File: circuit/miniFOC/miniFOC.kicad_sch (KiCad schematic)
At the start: 82 parts, among them J1 Conn_01x05, J2 Conn_01x03, J3 Conn_01x04, J4 Conn_01x02, J5 Conn_01x01, J6 Conn_01x01, J7 Conn_01x01, Q1 RU30J30M, Q2 RU30J30M, Q3 RU30J30M, U1 XC6206P332MR, U2 CH32V203C8T6, U3 LM321, U4 COS722MR, U5 BDR2L00, U6 BDR2L00, U7 BDR2L00, U8 JW5017S

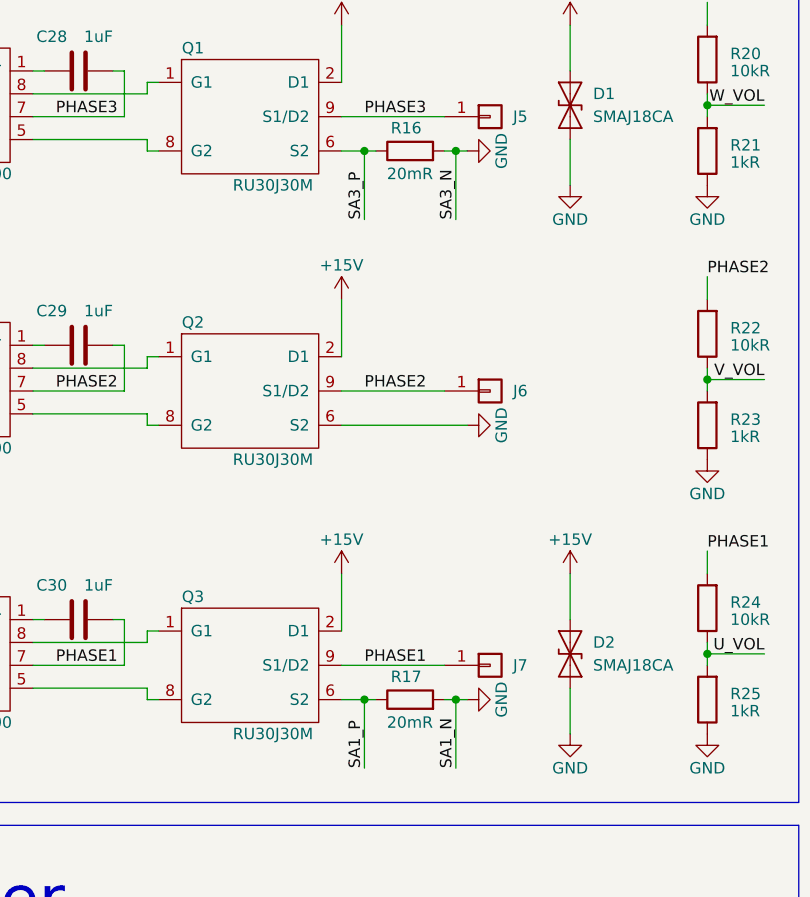
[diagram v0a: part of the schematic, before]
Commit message: Modify the sampling resistor package in the schematic diagram and PCB, and change its resistance value to 5 milliohms to adapt to the current sampling range of 20A.
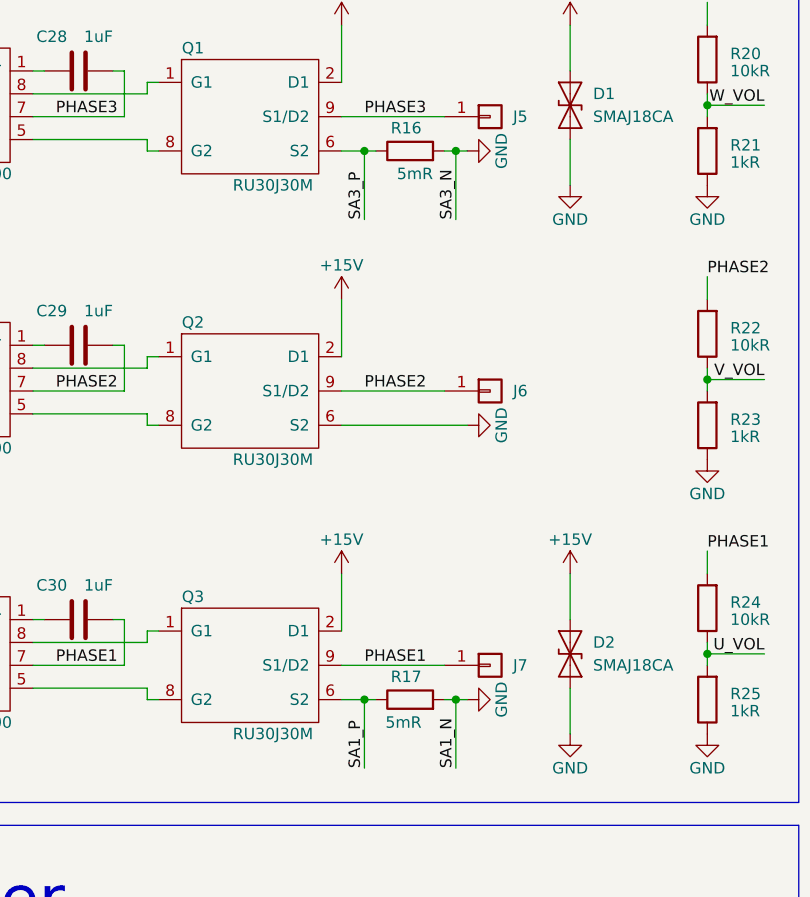
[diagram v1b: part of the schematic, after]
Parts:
- R16, R17: value 20mR -> 5mR; footprint library:R_0805_2012Metric -> library:R_1206_3216Metric
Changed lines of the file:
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@@
   (title_block
     (title "miniFOC")
-    (date "2023-06-20")
+    (date "2023-06-24")
     (rev "2.0.1")
   )
@@
       (effects (font (size 1.27 1.27)) (justify left))
     )
-    (property "Value" "20mR" (at 242.57 48.26 90)
+    (property "Value" "5mR" (at 242.57 48.26 90)
       (effects (font (size 1.27 1.27)) (justify left))
     )
-    (property "Footprint" "library:R_0805_2012Metric" (at 240.03 47.498 90)
+    (property "Footprint" "library:R_1206_3216Metric" (at 240.03 47.498 90)
       (effects (font (size 1.27 1.27)) hide)
     )
@@
       (effects (font (size 1.27 1.27)) (justify left))
     )
-    (property "Value" "20mR" (at 242.57 109.22 90)
+    (property "Value" "5mR" (at 241.3 109.22 90)
       (effects (font (size 1.27 1.27)) (justify left))
     )
-    (property "Footprint" "library:R_0805_2012Metric" (at 240.03 108.458 90)
+    (property "Footprint" "library:R_1206_3216Metric" (at 240.03 108.458 90)
       (effects (font (size 1.27 1.27)) hide)
     )

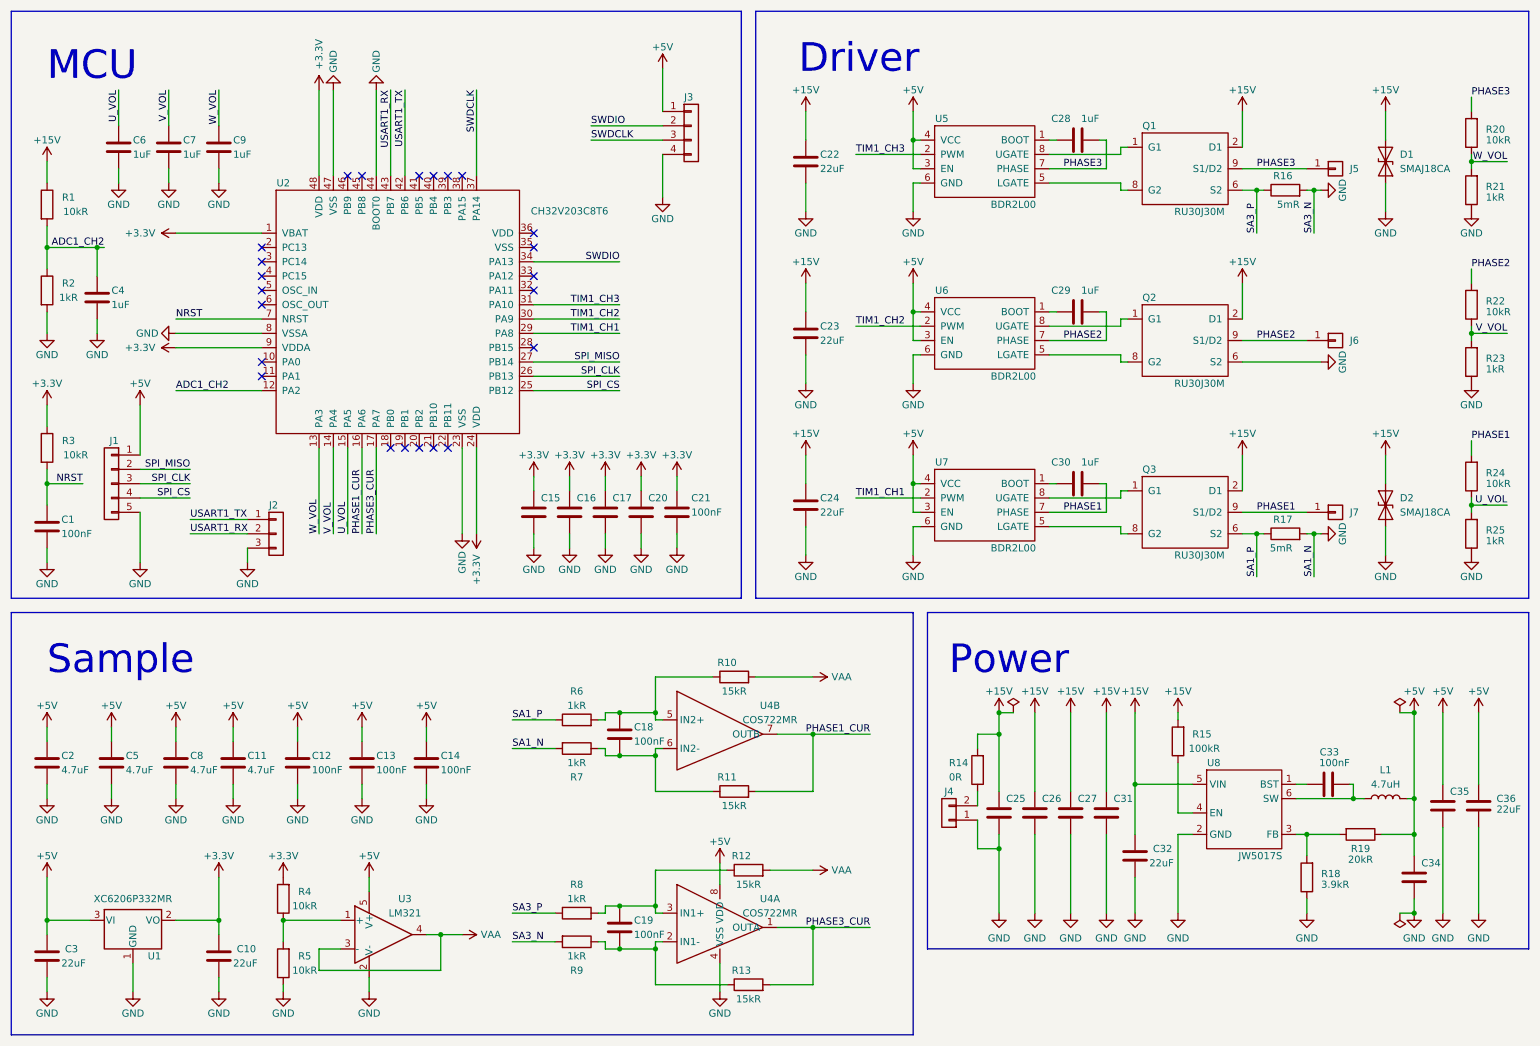
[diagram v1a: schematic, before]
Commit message: Updated PCB and schematic libraries to add buffer capacitors for current sampling.
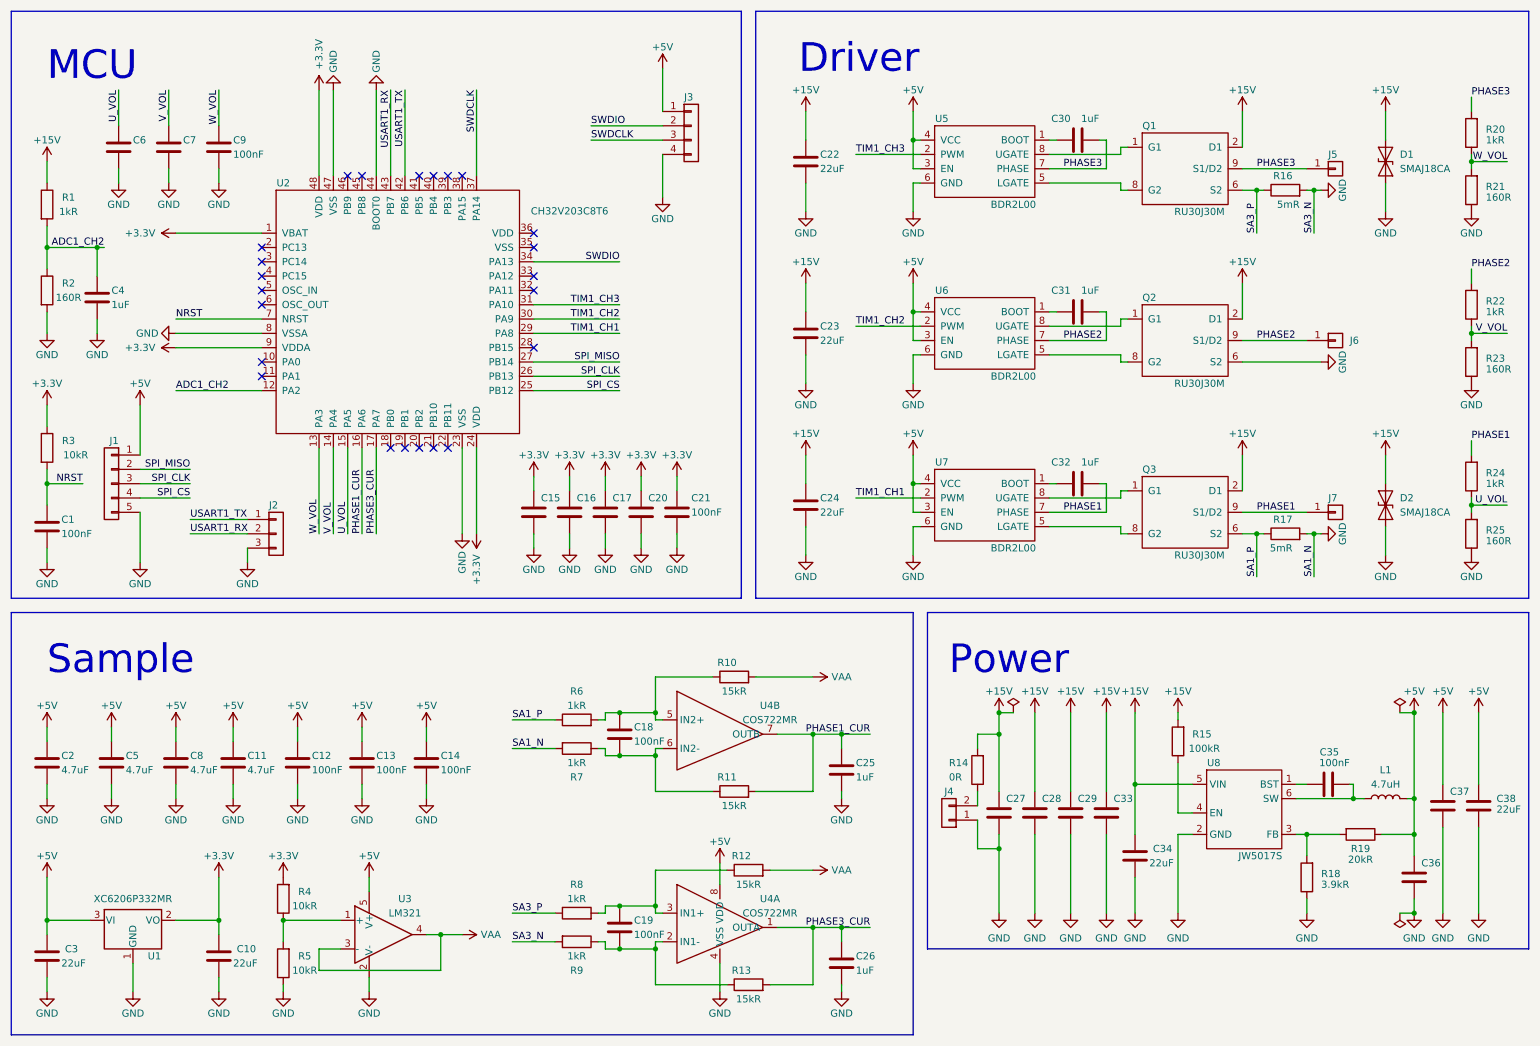
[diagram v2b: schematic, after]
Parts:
- added C25, C26: 1uF, library:C_0402_1005Metric, symbol library:C
- C6, C7, C9: value 1uF -> 100nF
- R1, R20, R22, R24: value 10kR -> 1kR
- R2, R21, R23, R25: value 1kR -> 160R
- renumbered C25 to C27, C26 to C28, C27 to C29, C28 to C30, C29 to C31, C30 to C32, C31 to C33, C32 to C34, C33 to C35, C34 to C36, C35 to C37, C36 to C38
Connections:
- net EP: now also C25.2, C26.2
- net PHASE1_CUR: now also C25.1
- net PHASE3_CUR: now also C26.1
